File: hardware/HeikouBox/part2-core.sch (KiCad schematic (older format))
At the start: 21 parts, among them J201 Conn_02x05_Odd_Even, J202 Conn_02x08_Odd_Even, U201 HeikouBox-Core, U202 74HCU04, Y201 14.31818MHz, Y202 28.37516MHz

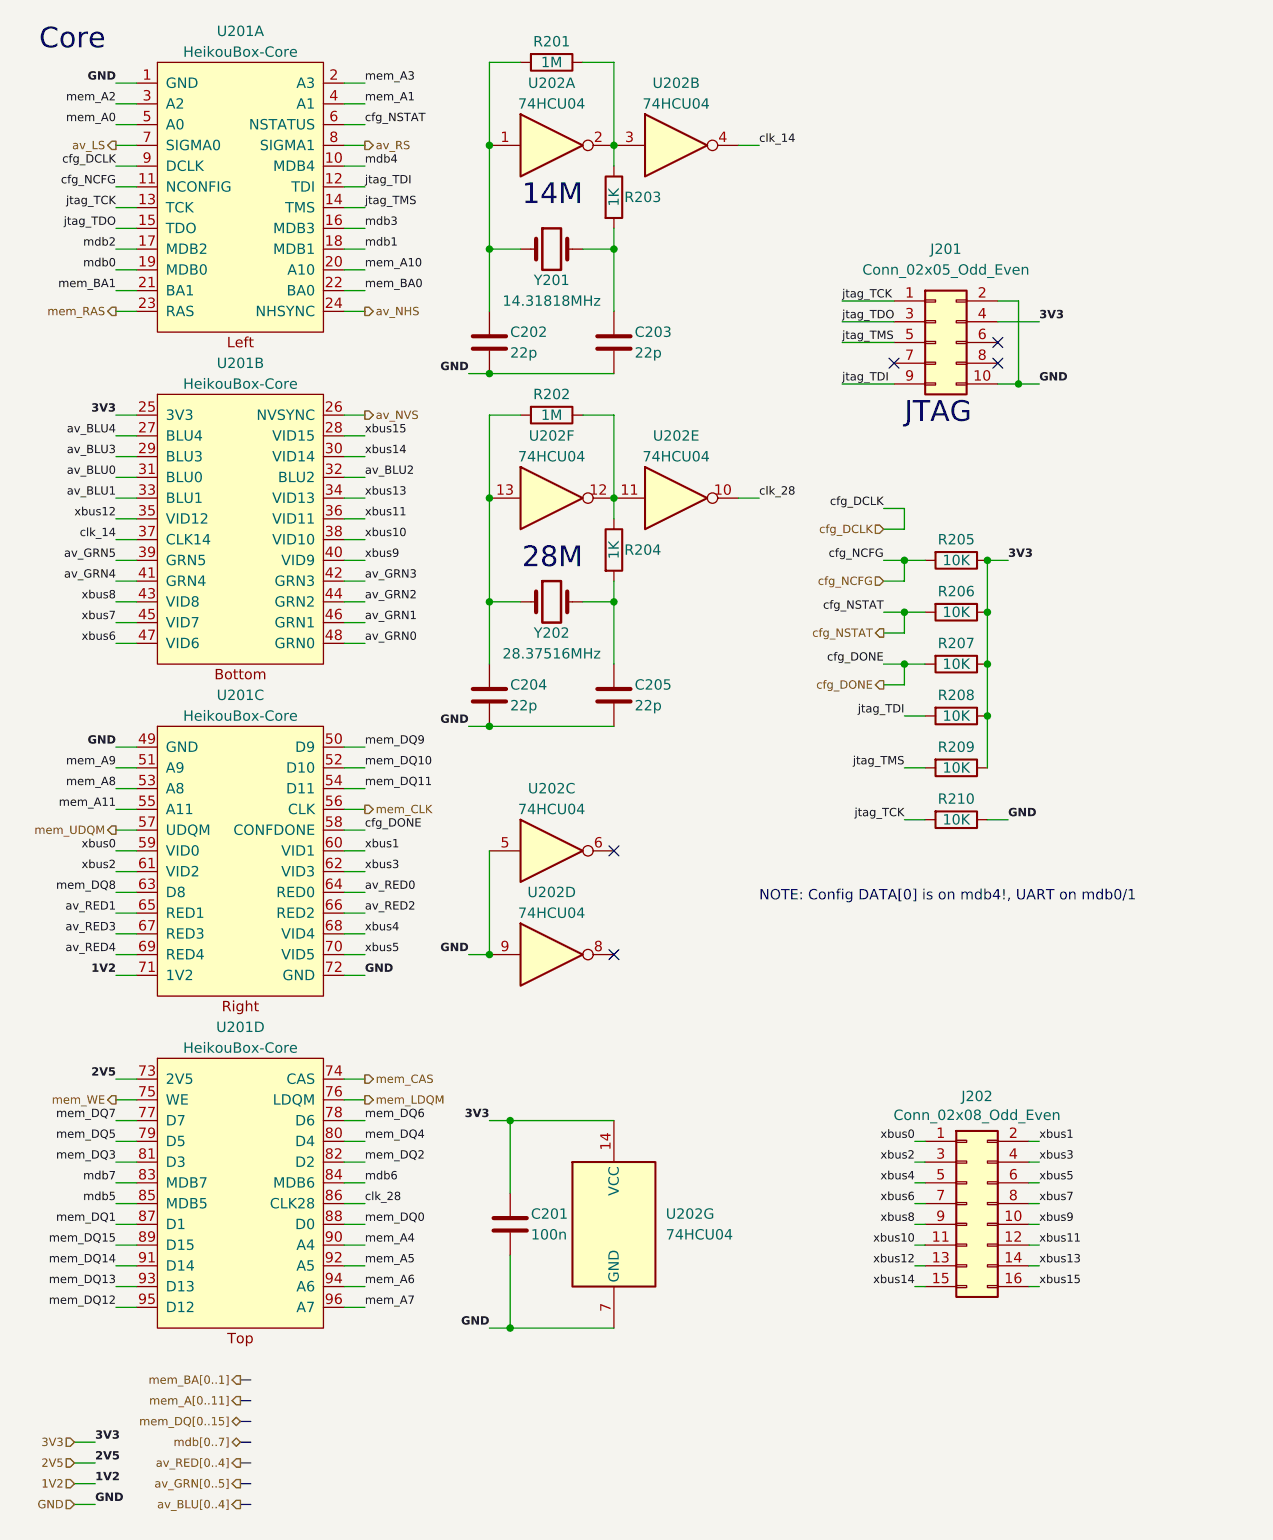
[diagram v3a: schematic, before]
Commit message: Connect UART correctly, remove unused mdb connection & mdb terminology
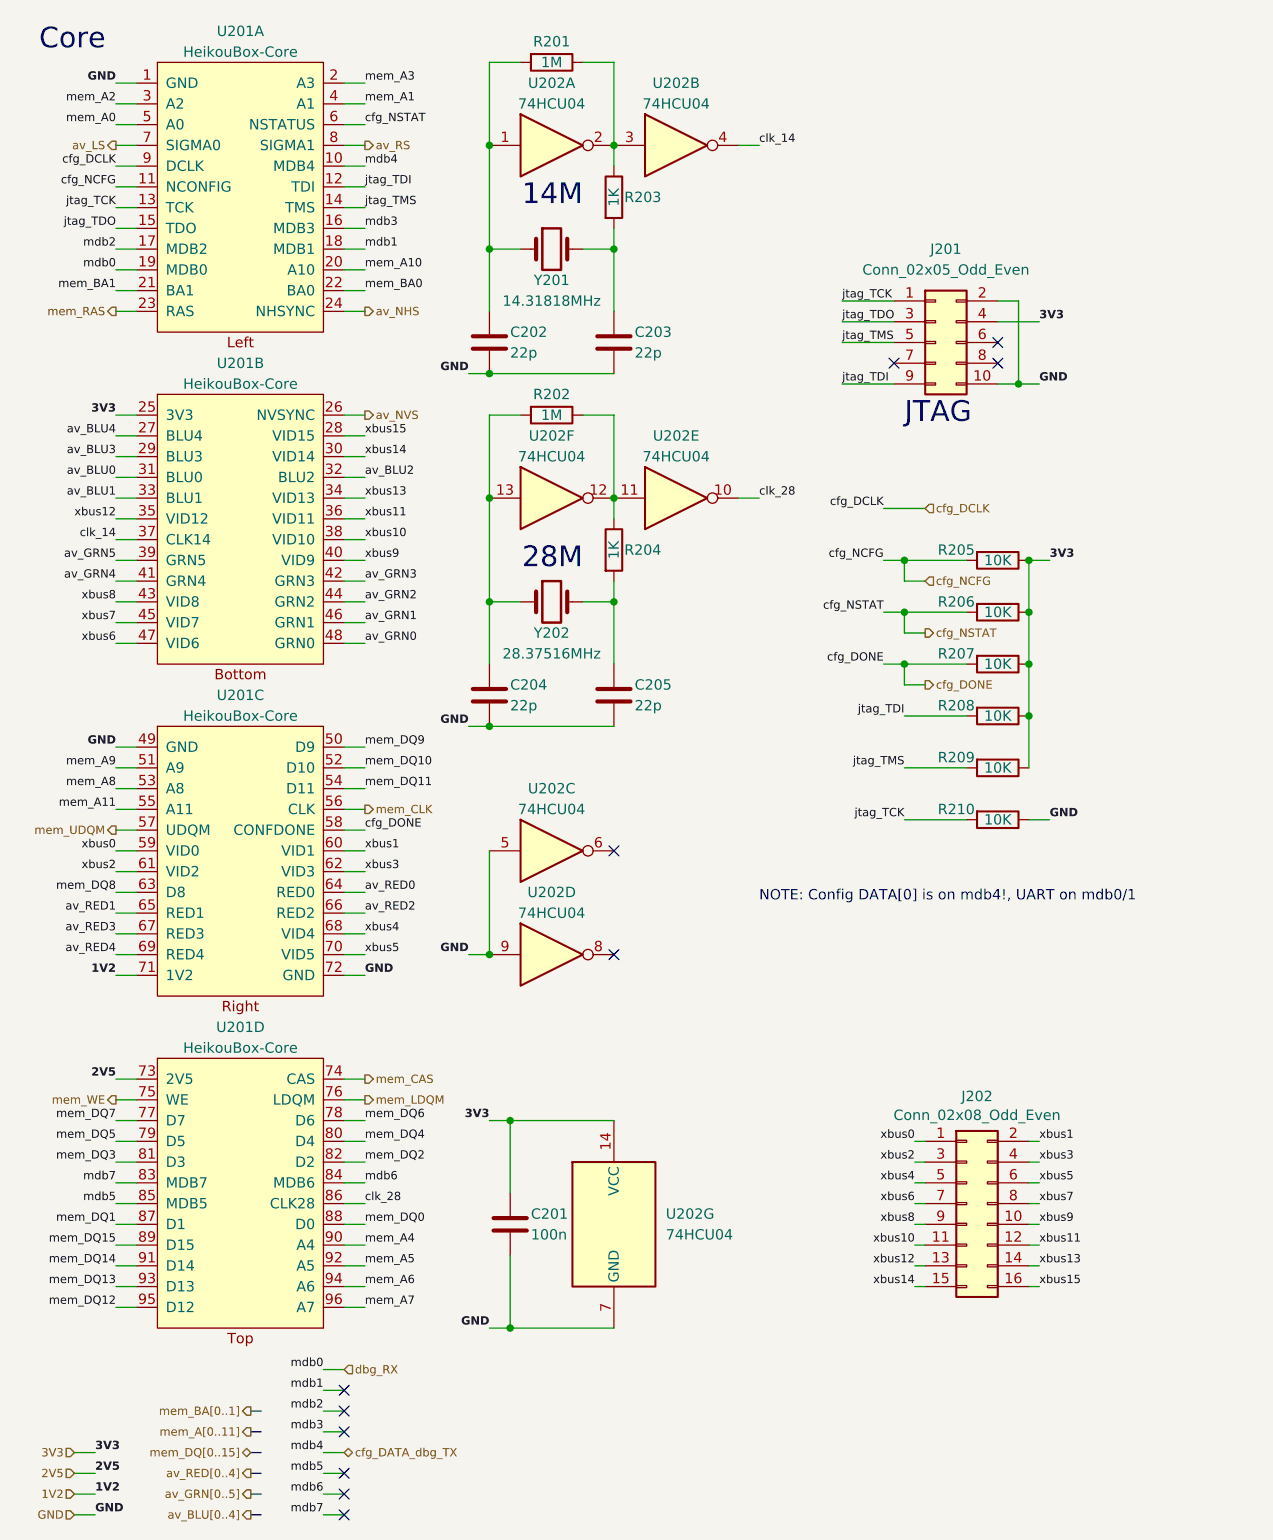
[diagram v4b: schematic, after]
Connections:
- net mdb0 renamed dbg_RX
- net mdb4 renamed cfg_DATA_dbg_TX
- no-connect marks 5 -> 11
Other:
- moved on the sheet: R205, R206, R207, R208, R209, R210
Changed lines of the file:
@@
 Comment4 ""
 $EndDescr
-Text HLabel 4600 2950 0    40   Input ~ 0
+Text HLabel 4800 2850 2    40   Input ~ 0
 cfg_DCLK
 $Comp
 L Device:R R?
 U 1 1 67C57990
-P 4950 3100
+P 5150 3100
 AR Path="/67C57990" Ref="R?"  Part="1"
 AR Path="/71351D1D/67C57990" Ref="R205"  Part="1"
 AR Path="/729F86A7/67C57990" Ref="R?"  Part="1"
-F 0 "R205" V 4850 3100 50  0000 C CNN
-F 1 "10K" V 4950 3100 50  0000 C CNN
-F 2 "Resistor_SMD:R_0603_1608Metric_Pad0.98x0.95mm_HandSolder" V 4880 3100 50  0001 C CNN
-F 3 "~" H 4950 3100 50  0001 C CNN
-	1    4950 3100
+F 0 "R205" V 5100 2900 50  0000 C CNN
+F 1 "10K" V 5150 3100 50  0000 C CNN
+F 2 "Resistor_SMD:R_0603_1608Metric_Pad0.98x0.95mm_HandSolder" V 5080 3100 50  0001 C CNN
+F 3 "~" H 5150 3100 50  0001 C CNN
+	1    5150 3100
 	0    1    1    0
 $EndComp
@@
 L Device:R R?
 U 1 1 67C57996
-P 4950 3350
+P 5150 3350
 AR Path="/67C57996" Ref="R?"  Part="1"
 AR Path="/71351D1D/67C57996" Ref="R206"  Part="1"
 AR Path="/729F86A7/67C57996" Ref="R?"  Part="1"
-F 0 "R206" V 4850 3350 50  0000 C CNN
-F 1 "10K" V 4950 3350 50  0000 C CNN
-F 2 "Resistor_SMD:R_0603_1608Metric_Pad0.98x0.95mm_HandSolder" V 4880 3350 50  0001 C CNN
-F 3 "~" H 4950 3350 50  0001 C CNN
-	1    4950 3350
+F 0 "R206" V 5100 3150 50  0000 C CNN
+F 1 "10K" V 5150 3350 50  0000 C CNN
+F 2 "Resistor_SMD:R_0603_1608Metric_Pad0.98x0.95mm_HandSolder" V 5080 3350 50  0001 C CNN
+F 3 "~" H 5150 3350 50  0001 C CNN
+	1    5150 3350
 	0    1    1    0
 $EndComp
@@
 L Device:R R?
 U 1 1 67C5799C
-P 4950 3600
+P 5150 3600
 AR Path="/67C5799C" Ref="R?"  Part="1"
 AR Path="/71351D1D/67C5799C" Ref="R207"  Part="1"
 AR Path="/729F86A7/67C5799C" Ref="R?"  Part="1"
-F 0 "R207" V 4850 3600 50  0000 C CNN
-F 1 "10K" V 4950 3600 50  0000 C CNN
-F 2 "Resistor_SMD:R_0603_1608Metric_Pad0.98x0.95mm_HandSolder" V 4880 3600 50  0001 C CNN
-F 3 "~" H 4950 3600 50  0001 C CNN
-	1    4950 3600
+F 0 "R207" V 5100 3400 50  0000 C CNN
+F 1 "10K" V 5150 3600 50  0000 C CNN
+F 2 "Resistor_SMD:R_0603_1608Metric_Pad0.98x0.95mm_HandSolder" V 5080 3600 50  0001 C CNN
+F 3 "~" H 5150 3600 50  0001 C CNN
+	1    5150 3600
 	0    1    1    0
 $EndComp
@@
 L Device:R R?
 U 1 1 67C579A2
-P 4950 3850
+P 5150 3850
 AR Path="/67C579A2" Ref="R?"  Part="1"
 AR Path="/71351D1D/67C579A2" Ref="R208"  Part="1"
 AR Path="/729F86A7/67C579A2" Ref="R?"  Part="1"
-F 0 "R208" V 4850 3850 50  0000 C CNN
-F 1 "10K" V 4950 3850 50  0000 C CNN
-F 2 "Resistor_SMD:R_0603_1608Metric_Pad0.98x0.95mm_HandSolder" V 4880 3850 50  0001 C CNN
-F 3 "~" H 4950 3850 50  0001 C CNN
-	1    4950 3850
+F 0 "R208" V 5100 3650 50  0000 C CNN
+F 1 "10K" V 5150 3850 50  0000 C CNN
+F 2 "Resistor_SMD:R_0603_1608Metric_Pad0.98x0.95mm_HandSolder" V 5080 3850 50  0001 C CNN
+F 3 "~" H 5150 3850 50  0001 C CNN
+	1    5150 3850
 	0    1    1    0
 $EndComp
@@
 L Device:R R?
 U 1 1 67C579A8
-P 4950 4100
+P 5150 4100
 AR Path="/67C579A8" Ref="R?"  Part="1"
 AR Path="/71351D1D/67C579A8" Ref="R209"  Part="1"
 AR Path="/729F86A7/67C579A8" Ref="R?"  Part="1"
-F 0 "R209" V 4850 4100 50  0000 C CNN
-F 1 "10K" V 4950 4100 50  0000 C CNN
-F 2 "Resistor_SMD:R_0603_1608Metric_Pad0.98x0.95mm_HandSolder" V 4880 4100 50  0001 C CNN
-F 3 "~" H 4950 4100 50  0001 C CNN
-	1    4950 4100
+F 0 "R209" V 5100 3900 50  0000 C CNN
+F 1 "10K" V 5150 4100 50  0000 C CNN
+F 2 "Resistor_SMD:R_0603_1608Metric_Pad0.98x0.95mm_HandSolder" V 5080 4100 50  0001 C CNN
+F 3 "~" H 5150 4100 50  0001 C CNN
+	1    5150 4100
 	0    1    1    0
 $EndComp
@@
 L Device:R R?
 U 1 1 67C579AE
-P 4950 4350
+P 5150 4350
 AR Path="/67C579AE" Ref="R?"  Part="1"
 AR Path="/71351D1D/67C579AE" Ref="R210"  Part="1"
 AR Path="/729F86A7/67C579AE" Ref="R?"  Part="1"
-F 0 "R210" V 4850 4350 50  0000 C CNN
-F 1 "10K" V 4950 4350 50  0000 C CNN
-F 2 "Resistor_SMD:R_0603_1608Metric_Pad0.98x0.95mm_HandSolder" V 4880 4350 50  0001 C CNN
-F 3 "~" H 4950 4350 50  0001 C CNN
-	1    4950 4350
+F 0 "R210" V 5100 4150 50  0000 C CNN
+F 1 "10K" V 5150 4350 50  0000 C CNN
+F 2 "Resistor_SMD:R_0603_1608Metric_Pad0.98x0.95mm_HandSolder" V 5080 4350 50  0001 C CNN
+F 3 "~" H 5150 4350 50  0001 C CNN
+	1    5150 4350
 	0    1    1    0
 $EndComp
 Wire Wire Line
-	4700 3100 4800 3100
-Wire Wire Line
-	4700 3350 4800 3350
-Wire Wire Line
-	4700 4350 4800 4350
+	4700 3100 5000 3100
+Wire Wire Line
+	4700 3350 5000 3350
+Wire Wire Line
+	4700 4350 5000 4350
 Text Notes 4700 2450 0    100  ~ 0
 JTAG
@@
 Text Notes 3150 1400 2    100  ~ 0
 14M
-Text HLabel 4600 3700 0    40   Output ~ 0
+Text HLabel 4800 3700 2    40   Output ~ 0
 cfg_DONE
 Wire Wire Line
-	4700 3850 4800 3850
-Wire Wire Line
-	4700 4100 4800 4100
-Text HLabel 4600 3450 0    40   Output ~ 0
+	4700 3850 5000 3850
+Wire Wire Line
+	4700 4100 5000 4100
+Text HLabel 4800 3450 2    40   Output ~ 0
 cfg_NSTAT
-Text HLabel 4600 3200 0    40   Input ~ 0
+Text HLabel 4800 3200 2    40   Input ~ 0
 cfg_NCFG
 Wire Wire Line
-	5100 4100 5100 3850
-Connection ~ 5100 3350
-Wire Wire Line
-	5100 3350 5100 3100
-Connection ~ 5100 3600
-Wire Wire Line
-	5100 3600 5100 3350
-Connection ~ 5100 3850
-Wire Wire Line
-	5100 3850 5100 3600
+	5300 4100 5300 3850
+Connection ~ 5300 3350
+Wire Wire Line
+	5300 3350 5300 3100
+Connection ~ 5300 3600
+Wire Wire Line
+	5300 3600 5300 3350
+Connection ~ 5300 3850
+Wire Wire Line
+	5300 3850 5300 3600
 Text Label 4400 1850 0    40   ~ 0
 jtag_TCK
@@
 NOTE: Config DATA[0] is on mdb4!, UART on mdb0/1
 Wire Bus Line
-	1550 7050 1500 7050
-Text HLabel 1500 7050 0    40   Output ~ 0
+	1600 7200 1550 7200
+Text HLabel 1550 7200 0    40   Output ~ 0
 mem_BA[0..1]
-Text HLabel 1500 7150 0    40   Output ~ 0
+Text HLabel 1550 7300 0    40   Output ~ 0
 mem_A[0..11]
 Wire Bus Line
-	1550 7150 1500 7150
-Text HLabel 1500 7250 0    40   BiDi ~ 0
+	1600 7300 1550 7300
+Text HLabel 1550 7400 0    40   BiDi ~ 0
 mem_DQ[0..15]
 Wire Bus Line
-	1550 7250 1500 7250
-Text HLabel 1500 7350 0    40   BiDi ~ 0
-mdb[0..7]
-Wire Bus Line
-	1550 7350 1500 7350
-Text HLabel 1500 7450 0    40   Output ~ 0
+	1600 7400 1550 7400
+Text HLabel 1550 7500 0    40   Output ~ 0
 av_RED[0..4]
-Text HLabel 1500 7550 0    40   Output ~ 0
+Text HLabel 1550 7600 0    40   Output ~ 0
 av_GRN[0..5]
-Text HLabel 1500 7650 0    40   Output ~ 0
+Text HLabel 1550 7700 0    40   Output ~ 0
 av_BLU[0..4]
 Wire Bus Line
-	1550 7450 1500 7450
+	1600 7500 1550 7500
 Wire Bus Line
-	1550 7550 1500 7550
+	1600 7600 1550 7600
 Wire Bus Line
-	1550 7650 1500 7650
+	1600 7700 1550 7700
 Wire Wire Line
 	2700 3900 3300 3900
@@
 Connection ~ 2700 5000
 Wire Wire Line
-	5100 4350 5200 4350
-Text Label 5200 4350 0    40   ~ 8
+	5300 4350 5400 4350
+Text Label 5400 4350 0    40   ~ 8
 GND
 Wire Wire Line
-	5100 3100 5200 3100
-Text Label 5200 3100 0    40   ~ 8
+	5300 3100 5400 3100
+Text Label 5400 3100 0    40   ~ 8
 3V3
-Connection ~ 5100 3100
+Connection ~ 5300 3100
 Wire Wire Line
 	2600 3900 2700 3900
@@
 	4700 3350 4700 3450
 Wire Wire Line
-	4700 3450 4600 3450
+	4700 3450 4800 3450
 Wire Wire Line
 	4600 3350 4700 3350
-Connection ~ 4700 3350
 Text Label 4600 3600 2    40   ~ 0
 cfg_DONE
@@
 	4600 3600 4700 3600
 Wire Wire Line
-	4600 3700 4700 3700
+	4800 3700 4700 3700
 Wire Wire Line
 	4700 3700 4700 3600
-Connection ~ 4700 3600
-Wire Wire Line
-	4700 3600 4800 3600
-Wire Wire Line
-	4600 3200 4700 3200
+Wire Wire Line
+	4700 3600 5000 3600
+Wire Wire Line
+	4800 3200 4700 3200
 Wire Wire Line
 	4700 3200 4700 3100
 Wire Wire Line
 	4600 3100 4700 3100
-Connection ~ 4700 3100
 Text Label 4600 3100 2    40   ~ 0
 cfg_NCFG
-Wire Wire Line
-	4600 2950 4700 2950
-Wire Wire Line
-	4700 2950 4700 2850
-Wire Wire Line
-	4700 2850 4600 2850
 Text Label 4600 2850 2    40   ~ 0
 cfg_DCLK
@@
 $EndComp
 Wire Wire Line
-	700  7550 800  7550
-Text Label 800  7550 0    40   ~ 8
+	700  7600 800  7600
+Text Label 800  7600 0    40   ~ 8
 1V2
-Text HLabel 700  7550 0    40   Input ~ 0
+Text HLabel 700  7600 0    40   Input ~ 0
 1V2
 Wire Wire Line
-	700  7450 800  7450
-Text Label 800  7450 0    40   ~ 8
+	700  7500 800  7500
+Text Label 800  7500 0    40   ~ 8
 2V5
-Text HLabel 700  7450 0    40   Input ~ 0
+Text HLabel 700  7500 0    40   Input ~ 0
 2V5
-Text Label 800  7650 0    40   ~ 8
+Text Label 800  7700 0    40   ~ 8
 GND
 Wire Wire Line
-	700  7350 800  7350
-Text Label 800  7350 0    40   ~ 8
+	700  7400 800  7400
+Text Label 800  7400 0    40   ~ 8
 3V3
-Text HLabel 700  7650 0    40   Input ~ 0
+Text HLabel 700  7700 0    40   Input ~ 0
 GND
 Wire Wire Line
-	700  7650 800  7650
-Text HLabel 700  7350 0    40   Input ~ 0
+	700  7700 800  7700
+Text HLabel 700  7400 0    40   Input ~ 0
 3V3
+Text Label 1900 7600 2    40   ~ 0
+mdb6
+Wire Wire Line
+	1900 7600 2000 7600
+Text Label 1900 7700 2    40   ~ 0
+mdb7
+Wire Wire Line
+	1900 7700 2000 7700
+Text Label 1900 7400 2    40   ~ 0
+mdb4
+Wire Wire Line
+	1900 7400 2000 7400
+Text Label 1900 7500 2    40   ~ 0
+mdb5
+Wire Wire Line
+	1900 7500 2000 7500
+Text Label 1900 7300 2    40   ~ 0
+mdb3
+Wire Wire Line
+	1900 7300 2000 7300
+Text Label 1900 7200 2    40   ~ 0
+mdb2
+Text Label 1900 7100 2    40   ~ 0
+mdb1
+Text Label 1900 7000 2    40   ~ 0
+mdb0
+Wire Wire Line
+	1900 7000 2000 7000
+Wire Wire Line
+	1900 7100 2000 7100
+Wire Wire Line
+	1900 7200 2000 7200
+NoConn ~ 2000 7100
+NoConn ~ 2000 7200
+NoConn ~ 2000 7300
+NoConn ~ 2000 7500
+NoConn ~ 2000 7600
+NoConn ~ 2000 7700
+Text HLabel 2000 7000 2    40   Input ~ 0
+dbg_RX
+Text HLabel 2000 7400 2    40   BiDi ~ 0
+cfg_DATA_dbg_TX
+Wire Wire Line
+	4600 2850 4800 2850
+Connection ~ 4700 3600
+Connection ~ 4700 3100
+Connection ~ 4700 3350
 $EndSCHEMATC
